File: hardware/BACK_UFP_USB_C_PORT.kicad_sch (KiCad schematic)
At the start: 30 parts, among them J7 USB4200-03-A (VIRT FLAG MOUNT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, Q18 PMPB09R5VPX, Q19 PMPB09R5VPX, Q20 PMPB09R5VPX, Q21 PMPB09R5VPX, U13 USB5926C, U15 PTN5100BMSP

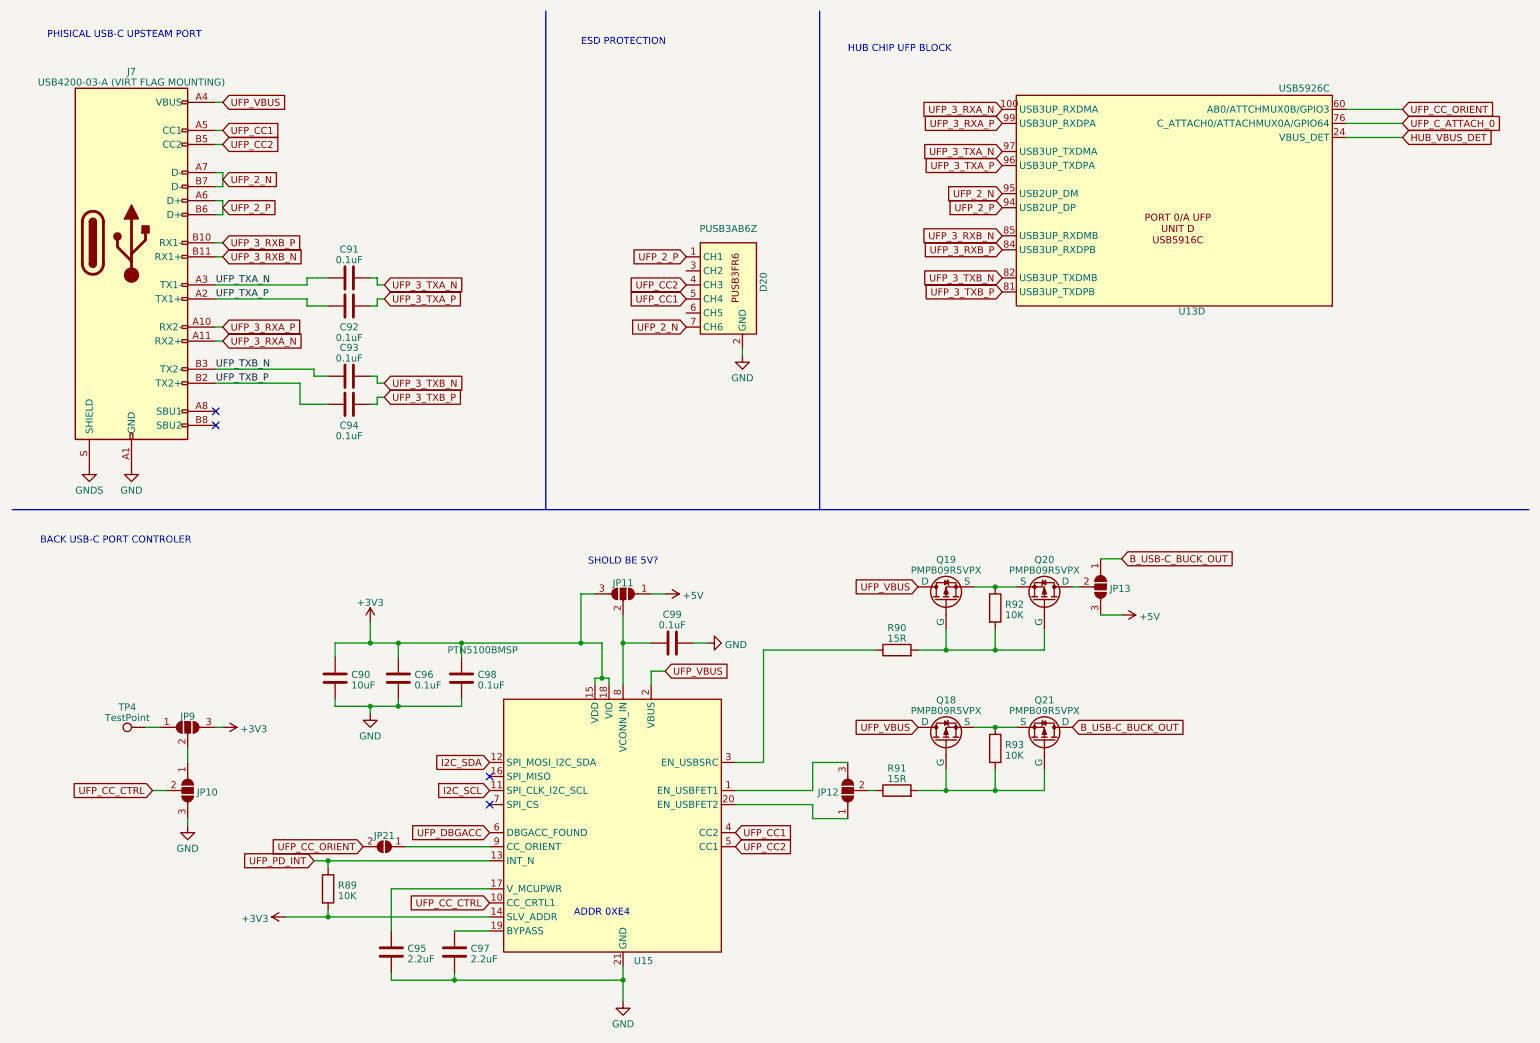
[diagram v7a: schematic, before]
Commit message: switched pd phy as old one needed an NDA
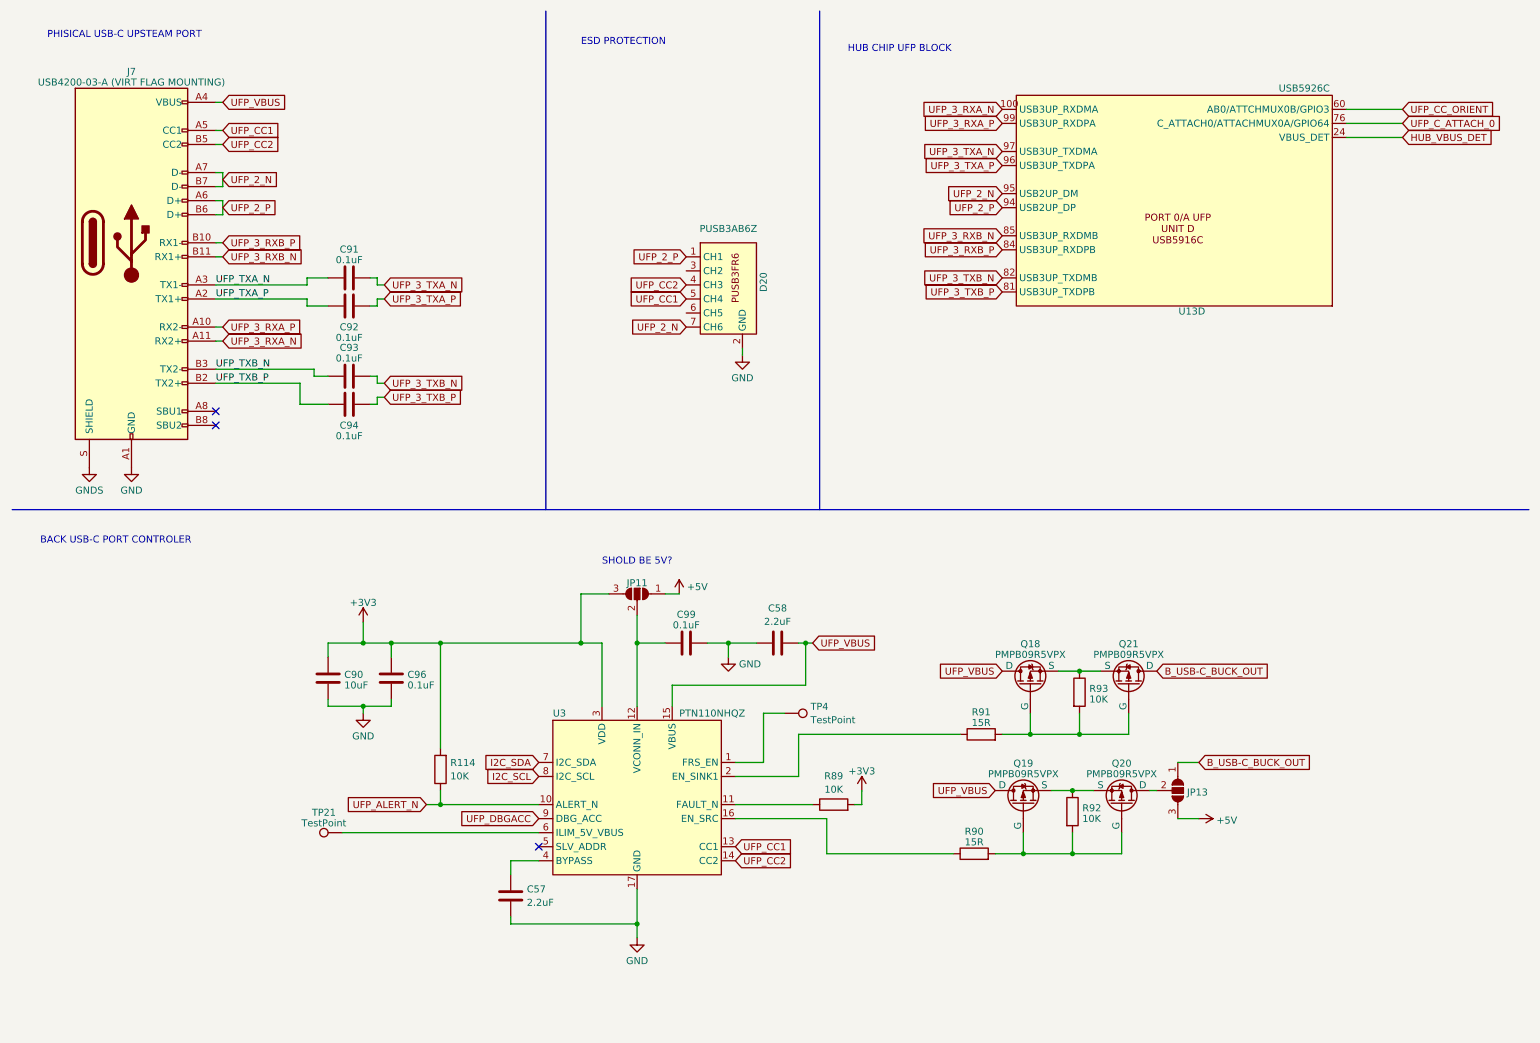
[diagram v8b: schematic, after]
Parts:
- removed C95, C97: 2.2uF, Capacitor_SMD:C_0603_1608Metric, symbol Device:C
- removed C98: 0.1uF, Capacitor_SMD:C_0603_1608Metric, symbol Device:C
- removed JP10, JP12, JP9: ~, Jumper:SolderJumper-3_P1.3mm_Open_RoundedPad1.0x1.5mm_NumberLabels, symbol Jumper:SolderJumper_3_Open
- removed JP21: ~, Jumper:SolderJumper-2_P1.3mm_Open_RoundedPad1.0x1.5mm, symbol Jumper:SolderJumper_2_Open
- removed U15: PTN5100BMSP, CARTHING:PTN5100BSMP, symbol CARTHING:PTN5100
- added C57, C58: 2.2uF, Capacitor_SMD:C_0603_1608Metric, symbol Device:C
- added R114: 10K, Resistor_SMD:R_0603_1608Metric, symbol Device:R
- added TP21: TestPoint, TestPoint:TestPoint_Pad_D1.5mm, symbol Connector:TestPoint
- added U3: PTN110NHQZ, CARTHING:PTN110, symbol CARTHING:PTN110
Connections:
- net +3V3: now also R114.2, U3.3 (VDD)
- net GND: now also C57.2, C58.1, U3.17 (GND)
- net I2C_SCL: now also U3.8 (I2C_SCL)
- net I2C_SDA: now also U3.7 (I2C_SDA)
- net UFP_CC1: now also U3.13 (CC1)
- net UFP_CC2: now also U3.14 (CC2)
- net UFP_DBGACC: now also U3.9 (DBG_ACC)
- net UFP_VBUS: now also C58.2, U3.15 (VBUS)
- net at R91.1: now also U3.2 (EN_SINK1)
- net at TP4.1: now also U3.1 (FRS_EN)
- net at R90.1: now also U3.16 (EN_SRC)
- net at C99.1, JP11.2 (C): now also U3.12 (VCONN_IN)
- net UFP_PD_INT: no longer names the net of R89.1
- net UFP_PD_INT: now also U3.11 (FAULT_N)
- new net: TP21.1, U3.6 (ILIM_5V_VBUS)
- new net: C57.1, U3.4 (BYPASS)
- new net UFP_ALERT_N: R114.1, U3.10 (ALERT_N)
- no-connect marks 4 -> 3
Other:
- note removed: "ADDR 0XE4"
- moved on the sheet: C90, C96, C99, JP11, JP13, Q18, Q19, Q20, Q21, R90, R91, R92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
